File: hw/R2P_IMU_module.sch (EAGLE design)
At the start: 32 parts, among them U1 STM32F103CX, U5 LD3985XX, X1 MICROMATCH-4

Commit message: Ongoing layout
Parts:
- added C10: 470n, rcl:C-EUC0603
- added C13: 10n, rcl:C-EUC0603
- added C14: 220n, rcl:C-EUC0603
- added C15: 4.7u, rcl:C-EUC0805
- added C16, C2, C4: 10u, rcl:C-EUC0805
- added C17, C3, C8: 100n, rcl:C-EUC0603
- added R5: 10k, rcl:R-EU_R0603
- added R6, R7: 2.7k, rcl:R-EU_R0603
- added U$2: LPS331AP, st:LPS331AP
- added U2: L3G4200D, st:L3G4200D
- added U6: LSM303DLHC, st:LSM303DLHC
- added X2: MICROMATCH-6, tyco:MICROMATCH-6
- X1: device con-amp-micromatch:MICROMATCH-4 -> tyco:MICROMATCH-4
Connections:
- new net BAR_CS: U$2.CS
- new net BAR_INT1: U$2.INT1
- new net BAR_INT2: U$2.INT2
- new net N$10: C10.1, C13.1, U2.PLLFILT
- new net N$14: C14.1, U6.SETP
- new net N$16: C14.2, U6.SETC
- new net N$17: C15.1, U6.C1
- new net N$9: C10.2, R5.1
- net +3V3: now also C16.1, C17.1, C2.1, C3.1, C4.1, C8.1, R6.1, R7.1, U$2.VCCA, U$2.VDD, U$2.VDD_IO, U2.RES6, U2.VDD, U2.VDD_IO, U6.VDD, U6.VDD_IO, X2-3.S
- net AM_DRDY: now also U6.DRDY
- net AM_INT1: now also U6.INT1
- net AM_INT2: now also U6.INT2
- net GND: now also C13.2, C15.2, C16.2, C17.2, C2.2, C3.2, C4.2, C8.2, R5.2, U$2.GND_1, U$2.GND_2, U$2.GND_3, U$2.GND_4, U$2.RES, U2.GND, U2.RES1, U2.RES2, U2.RES3, U2.RES4, U2.RES5, U6.GND, U6.RES1, U6.RES2, X2-1.S
- net GPS_RESET: now also X2-5.S
- net GPS_RX: now also X2-2.S
- net GPS_STATUS: now also X2-6.S
- net GPS_TX: now also X2-4.S
- net GYRO_CS: now also U2.CS
- net GYRO_INT1: now also U2.INT1
- net GYRO_INT2: now also U2.INT2
- net MISO: now also U$2.SDO, U2.SDO
- net MOSI: now also U$2.SDA/SDI, U2.SDI
- net SCK: now also U$2.SCL, U2.SCL
- net SCL: now also R7.2, U6.SCL
- net SDA: now also R6.2, U6.SDA
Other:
- note added: "ACCELEROMETER WITH MAGNETOMETER"
- note added: "GYRO"
- moved on the sheet: X1-1, X1-2, X1-3, X1-4

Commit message: Board layout finished
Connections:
- removed net N$1: U$4.P$5
- removed net OSC_OUT: U1.PD1/OSC_OUT
- net +3V3: now also X2-1.S; no longer X2-3.S
- net BAR_CS: now also U1.PC15
- net BAR_INT1: now also U1.PC13
- net BAR_INT2: now also U1.PC14
- net GND: now also U$4.P$5, X2-2.S; no longer X2-1.S
- net GPS_RX: now also X2-4.S; no longer X2-2.S
- net GPS_TX: now also X2-3.S; no longer X2-4.S
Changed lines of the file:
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@@
 </segment>
 <segment>
-<wire x1="25.4" y1="78.74" x2="20.32" y2="78.74" width="0.1524" layer="91"/>
+<wire x1="25.4" y1="78.74" x2="22.86" y2="78.74" width="0.1524" layer="91"/>
 <pinref part="U$4" gate="G$1" pin="P$3"/>
 <pinref part="GND2" gate="1" pin="GND"/>
+<wire x1="22.86" y1="78.74" x2="20.32" y2="78.74" width="0.1524" layer="91"/>
+<wire x1="25.4" y1="76.2" x2="22.86" y2="76.2" width="0.1524" layer="91"/>
+<wire x1="22.86" y1="76.2" x2="22.86" y2="78.74" width="0.1524" layer="91"/>
+<pinref part="U$4" gate="G$1" pin="P$5"/>
+<junction x="22.86" y="78.74"/>
 </segment>
 <segment>
@@
 </segment>
 <segment>
-<wire x1="320.04" y1="223.52" x2="314.96" y2="223.52" width="0.1524" layer="91"/>
-<label x="309.88" y="223.52" size="1.778" layer="95"/>
-<pinref part="X2" gate="-1" pin="S"/>
-</segment>
-<segment>
 <pinref part="GND32" gate="1" pin="GND"/>
 <pinref part="C2" gate="G$1" pin="2"/>
@@
 <wire x1="175.26" y1="99.06" x2="175.26" y2="96.52" width="0.1524" layer="91"/>
 <pinref part="GND33" gate="1" pin="GND"/>
+</segment>
+<segment>
+<wire x1="320.04" y1="220.98" x2="314.96" y2="220.98" width="0.1524" layer="91"/>
+<label x="304.8" y="220.98" size="1.778" layer="95"/>
+<pinref part="X2" gate="-2" pin="S"/>
 </segment>
 </net>
@@
 <wire x1="99.06" y1="243.84" x2="106.68" y2="243.84" width="0.1524" layer="91"/>
 <junction x="106.68" y="243.84"/>
+<junction x="121.92" y="243.84"/>
 </segment>
 <segment>
@@
 </segment>
 <segment>
-<wire x1="320.04" y1="218.44" x2="314.96" y2="218.44" width="0.1524" layer="91"/>
-<label x="309.88" y="218.44" size="1.778" layer="95"/>
-<pinref part="X2" gate="-3" pin="S"/>
-</segment>
-<segment>
 <wire x1="271.78" y1="241.3" x2="271.78" y2="243.84" width="0.1524" layer="91"/>
 <pinref part="R6" gate="G$1" pin="1"/>
@@
 <junction x="210.82" y="114.3"/>
 </segment>
+<segment>
+<wire x1="320.04" y1="223.52" x2="314.96" y2="223.52" width="0.1524" layer="91"/>
+<label x="304.8" y="223.52" size="1.778" layer="95"/>
+<pinref part="X2" gate="-1" pin="S"/>
+</segment>
 </net>
 <net name="JTMS" class="0">
@@
 </segment>
 </net>
-<net name="OSC_OUT" class="0">
-<segment>
-<wire x1="48.26" y1="236.22" x2="48.26" y2="238.76" width="0.1524" layer="91"/>
-<label x="48.26" y="238.76" size="1.778" layer="95" rot="R90"/>
-<pinref part="U1" gate="G$1" pin="PD1/OSC_OUT"/>
-</segment>
-</net>
 <net name="NRST" class="0">
 <segment>
@@
 <label x="45.72" y="71.12" size="1.778" layer="95"/>
 <pinref part="U$4" gate="G$1" pin="P$10"/>
-</segment>
-</net>
-<net name="N$1" class="0">
-<segment>
-<wire x1="25.4" y1="76.2" x2="22.86" y2="76.2" width="0.1524" layer="91"/>
-<wire x1="22.86" y1="76.2" x2="22.86" y2="78.74" width="0.1524" layer="91"/>
-<pinref part="U$4" gate="G$1" pin="P$5"/>
 </segment>
 </net>
@@
 <label x="276.86" y="200.66" size="1.778" layer="95"/>
 <pinref part="R7" gate="G$1" pin="2"/>
+<junction x="271.78" y="200.66"/>
 </segment>
 </net>
@@
 <label x="276.86" y="228.6" size="1.778" layer="95"/>
 <pinref part="R6" gate="G$1" pin="2"/>
+<junction x="271.78" y="228.6"/>
 </segment>
 </net>
@@
 </segment>
 <segment>
+<wire x1="320.04" y1="218.44" x2="314.96" y2="218.44" width="0.1524" layer="91"/>
+<label x="304.8" y="218.44" size="1.778" layer="95"/>
+<pinref part="X2" gate="-3" pin="S"/>
+</segment>
+</net>
+<net name="GPS_RX" class="0">
+<segment>
+<wire x1="25.4" y1="193.04" x2="22.86" y2="193.04" width="0.1524" layer="91"/>
+<label x="15.24" y="193.04" size="1.778" layer="95"/>
+<pinref part="U1" gate="G$1" pin="PA3"/>
+</segment>
+<segment>
 <wire x1="320.04" y1="215.9" x2="314.96" y2="215.9" width="0.1524" layer="91"/>
 <label x="304.8" y="215.9" size="1.778" layer="95"/>
 <pinref part="X2" gate="-4" pin="S"/>
-</segment>
-</net>
-<net name="GPS_RX" class="0">
-<segment>
-<wire x1="25.4" y1="193.04" x2="22.86" y2="193.04" width="0.1524" layer="91"/>
-<label x="15.24" y="193.04" size="1.778" layer="95"/>
-<pinref part="U1" gate="G$1" pin="PA3"/>
-</segment>
-<segment>
-<wire x1="320.04" y1="220.98" x2="314.96" y2="220.98" width="0.1524" layer="91"/>
-<label x="304.8" y="220.98" size="1.778" layer="95"/>
-<pinref part="X2" gate="-2" pin="S"/>
 </segment>
 </net>
@@
 <label x="162.56" y="101.6" size="1.778" layer="95"/>
 </segment>
+<segment>
+<pinref part="U1" gate="G$1" pin="PC14"/>
+<wire x1="55.88" y1="236.22" x2="55.88" y2="238.76" width="0.1524" layer="91"/>
+<label x="55.88" y="238.76" size="1.778" layer="95" rot="R90"/>
+</segment>
 </net>
 <net name="BAR_INT1" class="0">
@@
 <label x="162.56" y="104.14" size="1.778" layer="95"/>
 </segment>
+<segment>
+<pinref part="U1" gate="G$1" pin="PC13"/>
+<wire x1="58.42" y1="236.22" x2="58.42" y2="238.76" width="0.1524" layer="91"/>
+<label x="58.42" y="238.76" size="1.778" layer="95" rot="R90"/>
+</segment>
 </net>
 <net name="BAR_CS" class="0">
@@
 <label x="162.56" y="114.3" size="1.778" layer="95"/>
 </segment>
-</net>
+<segment>
+<pinref part="U1" gate="G$1" pin="PC15"/>
+<wire x1="53.34" y1="236.22" x2="53.34" y2="238.76" width="0.1524" layer="91"/>
+<label x="53.34" y="238.76" size="1.778" layer="95" rot="R90"/>
+</segment>
+</net>

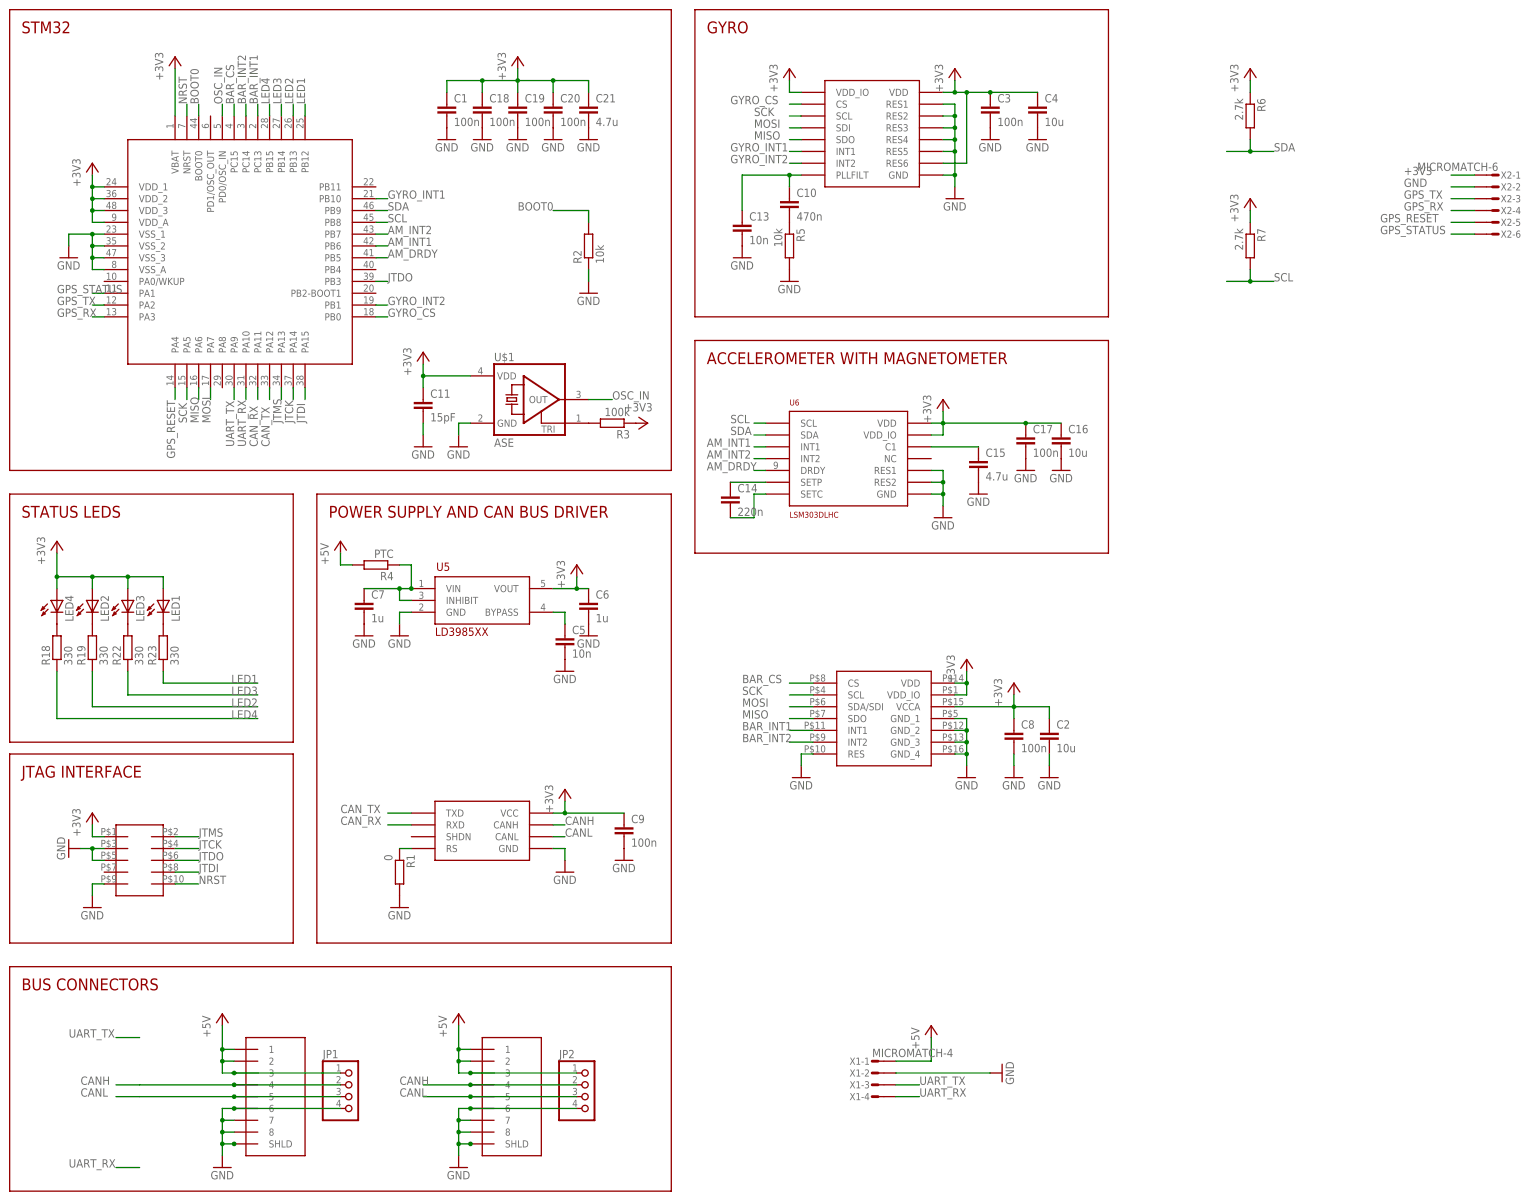
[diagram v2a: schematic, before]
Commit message: schematics reorganized
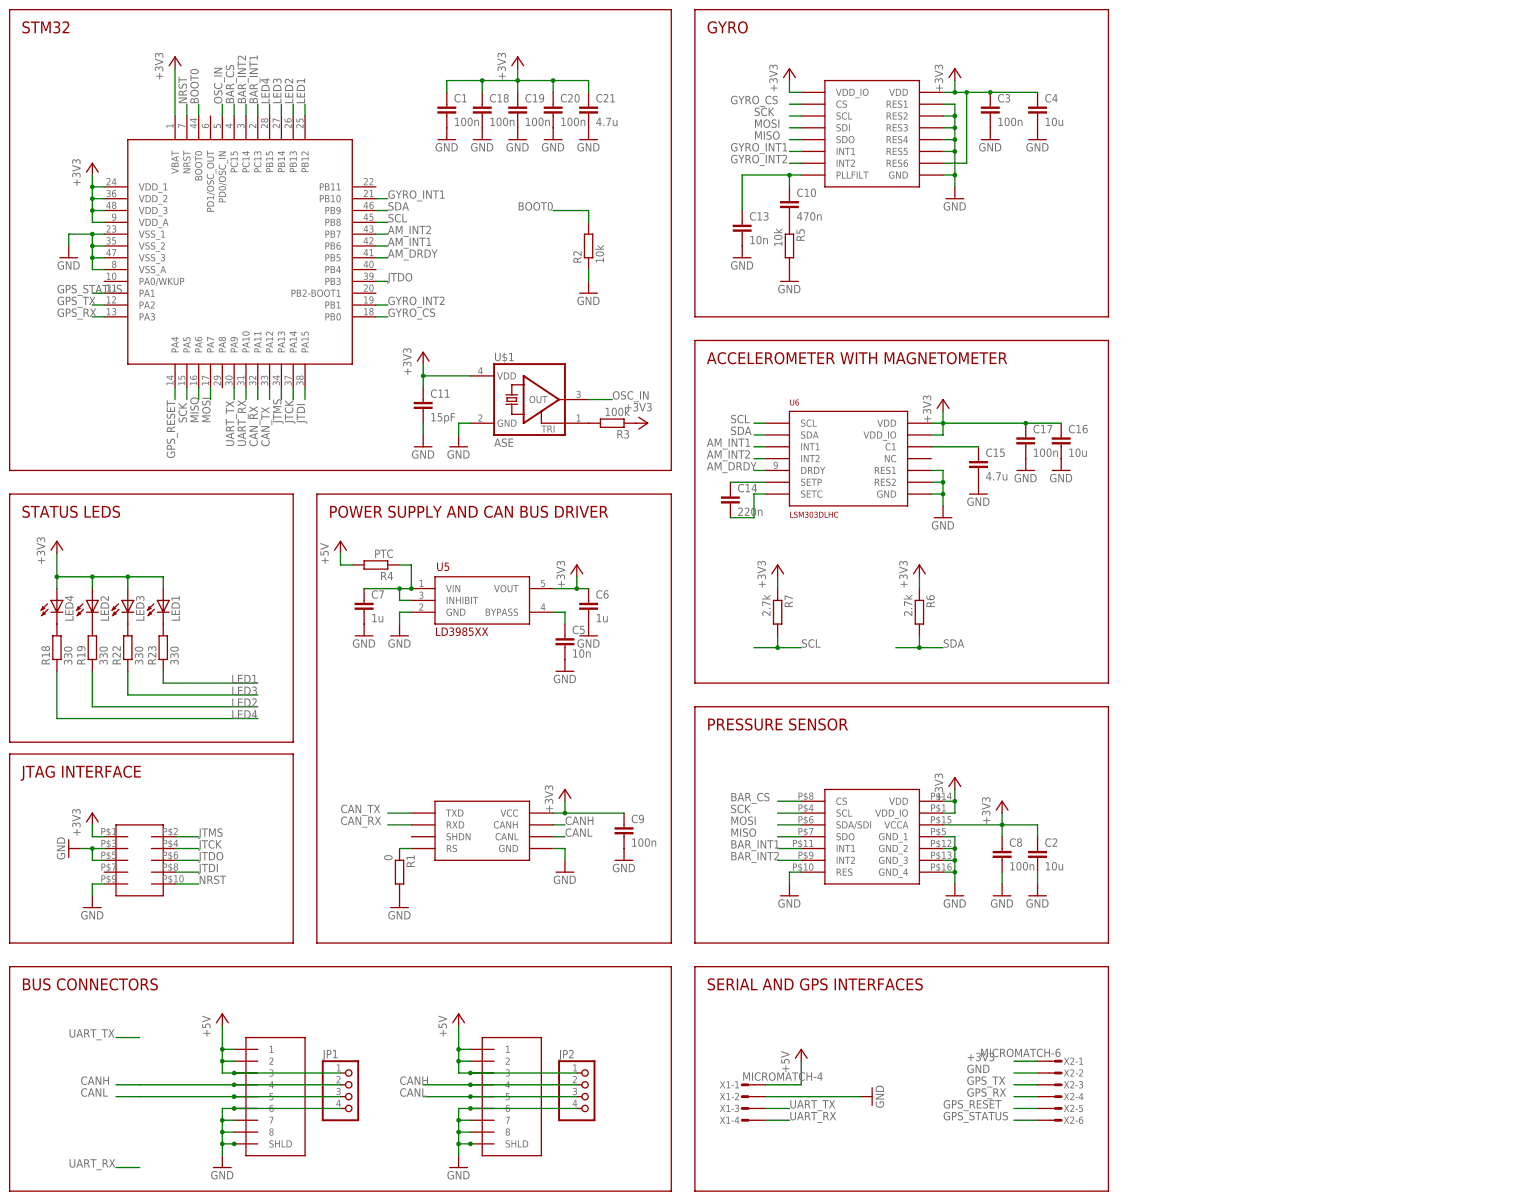
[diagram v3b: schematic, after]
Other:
- note added: "PRESSURE SENSOR"
- note added: "SERIAL AND GPS INTERFACES"
- moved on the sheet: C2, C8, R6, R7, X1-1, X1-2, X1-3, X1-4, X2-1, X2-2, X2-3, X2-4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
